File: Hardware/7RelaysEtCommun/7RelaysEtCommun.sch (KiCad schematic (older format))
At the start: 41 parts, among them J1 5VIN, J10 ISP, J2 Conn_01x02_Female, J3 Conn_01x02_Female, J4 Conn_01x02_Female, J5 Conn_01x02_Female, J6 Conn_01x02_Female, J7 Conn_01x02_Female, J8 Conn_01x02_Female, K1 UMS05-1A80-75L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

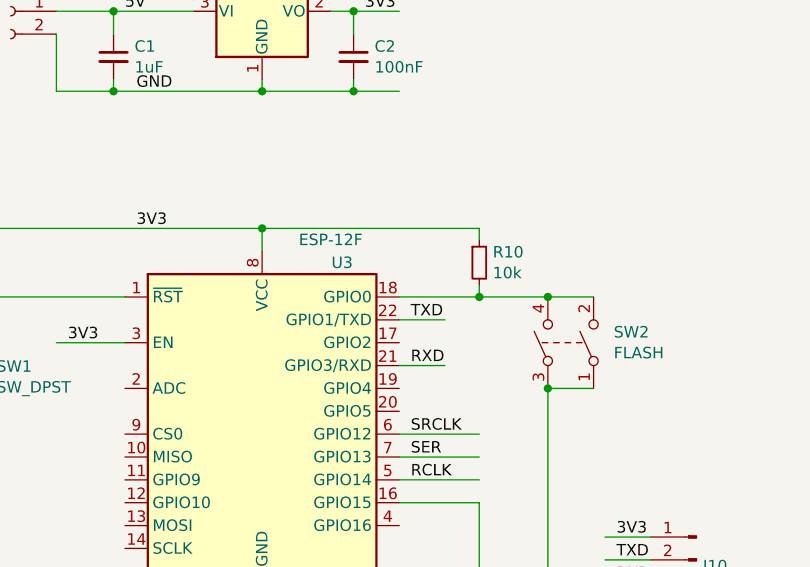
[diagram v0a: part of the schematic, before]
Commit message: - Modified almost all hardware boards : They were missing a pull-up resistor on GPIO2, which made impossible to flash. - Updated baseBoard.* files
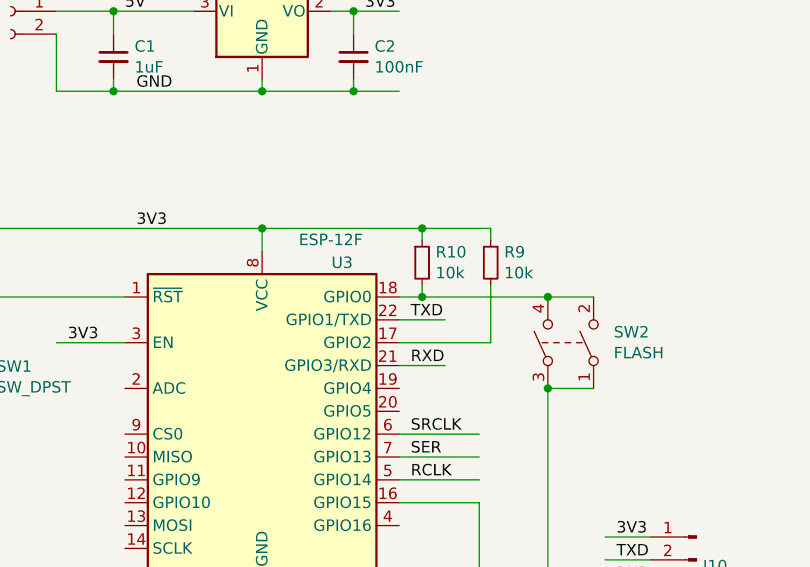
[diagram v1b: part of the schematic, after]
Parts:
- added R9: 10k, Resistor_SMD:R_0805_2012Metric_Pad1.15x1.40mm_HandSolder, symbol Device:R_Small
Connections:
- wire segments 160 -> 164
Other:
- moved on the sheet: R10
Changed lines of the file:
@@
 3V3
-Wire Wire Line
-	2650 2000 3000 2000
-Wire Wire Line
-	3000 1700 2050 1700
-Connection ~ 2050 1700
 Wire Wire Line
 	2650 2900 3000 2900
@@
 L Device:R_Small R10
 U 1 1 5BB64501
-P 3000 1850
-F 0 "R10" H 3059 1896 50  0000 L CNN
-F 1 "10k" H 3059 1805 50  0000 L CNN
-F 2 "Resistor_SMD:R_0805_2012Metric_Pad1.15x1.40mm_HandSolder" H 3000 1850 50  0001 C CNN
-F 3 "~" H 3000 1850 50  0001 C CNN
-	1    3000 1850
+P 2750 1850
+F 0 "R10" H 2809 1896 50  0000 L CNN
+F 1 "10k" H 2809 1805 50  0000 L CNN
+F 2 "Resistor_SMD:R_0805_2012Metric_Pad1.15x1.40mm_HandSolder" H 2750 1850 50  0001 C CNN
+F 3 "~" H 2750 1850 50  0001 C CNN
+	1    2750 1850
 	1    0    0    -1
 $EndComp
@@
 	0    -1   -1   0
 $EndComp
-Wire Wire Line
-	3000 1750 3000 1700
-Wire Wire Line
-	3000 1950 3000 2000
-Wire Wire Line
-	3000 2000 3300 2000
-Connection ~ 3000 2000
 Wire Wire Line
 	3300 2000 3500 2000
@@
 Text Label 7000 4100 0    50   ~ 0
 NE
+Wire Wire Line
+	2650 2000 2750 2000
+$Comp
+L Device:R_Small R9
+U 1 1 5C8243B1
+P 3050 1850
+F 0 "R9" H 3109 1896 50  0000 L CNN
+F 1 "10k" H 3109 1805 50  0000 L CNN
+F 2 "Resistor_SMD:R_0805_2012Metric_Pad1.15x1.40mm_HandSolder" H 3050 1850 50  0001 C CNN
+F 3 "~" H 3050 1850 50  0001 C CNN
+	1    3050 1850
+	1    0    0    -1
+$EndComp
+Wire Wire Line
+	2750 2000 2750 1950
+Connection ~ 2750 2000
+Wire Wire Line
+	2750 2000 3300 2000
+Wire Wire Line
+	2050 1700 2750 1700
+Wire Wire Line
+	3050 1700 3050 1750
+Connection ~ 2050 1700
+Wire Wire Line
+	2750 1750 2750 1700
+Connection ~ 2750 1700
+Wire Wire Line
+	2750 1700 3050 1700
+Wire Wire Line
+	3050 1950 3050 2200
+Wire Wire Line
+	3050 2200 2650 2200
 $EndSCHEMATC
